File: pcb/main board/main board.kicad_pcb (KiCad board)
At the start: 2 copper layers, 110 x 155 mm, 71 parts, among them J1 Motor 0 Conn, J10 12V Battery, J11 BAU, J12 Servo 4 Conn, J13 Servo 1 Conn, J14 Servo 2 Conn, J15 Servo 3 Conn, J16 Servo 5 Conn, J17 Servo 6 Conn, J18 Servo 7 Conn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

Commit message: Finished PCB !
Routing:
- net +5VP: track 151.5 -> 353.7 mm, vias 2 -> 12
- net +12V: track 302.5 -> 356.2 mm, vias 10 -> 11
- net I2C 0 SDA: track 74.0 -> 96.9 mm, vias 2 -> 4
- net I2C 0 SCL: track 86.2 -> 108.0 mm, vias 4 -> 5
- net +5VL: track 325.6 -> 324.0 mm

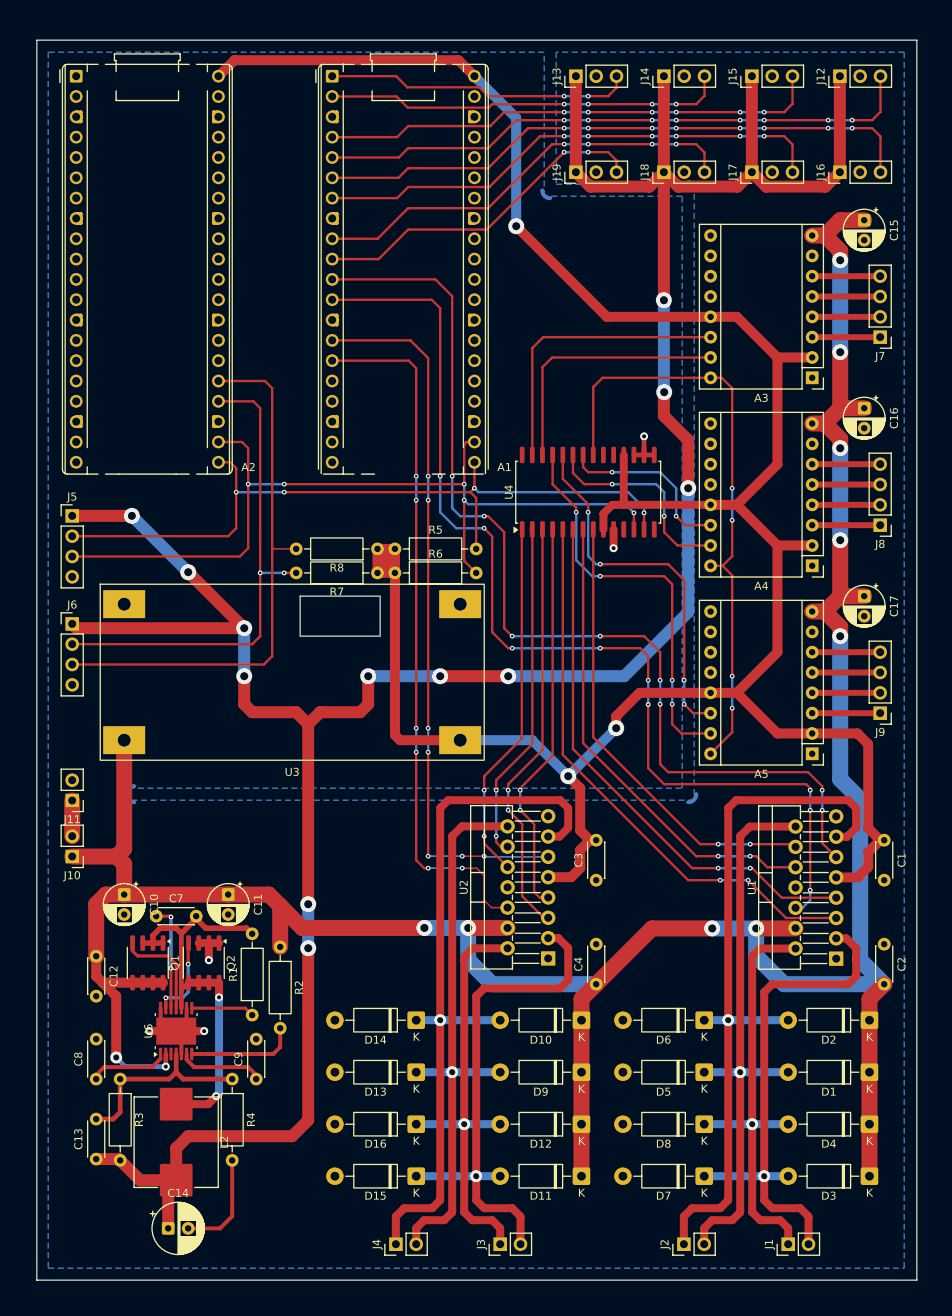
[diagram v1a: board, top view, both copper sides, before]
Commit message: Added Aisler DRC and corrected errors.
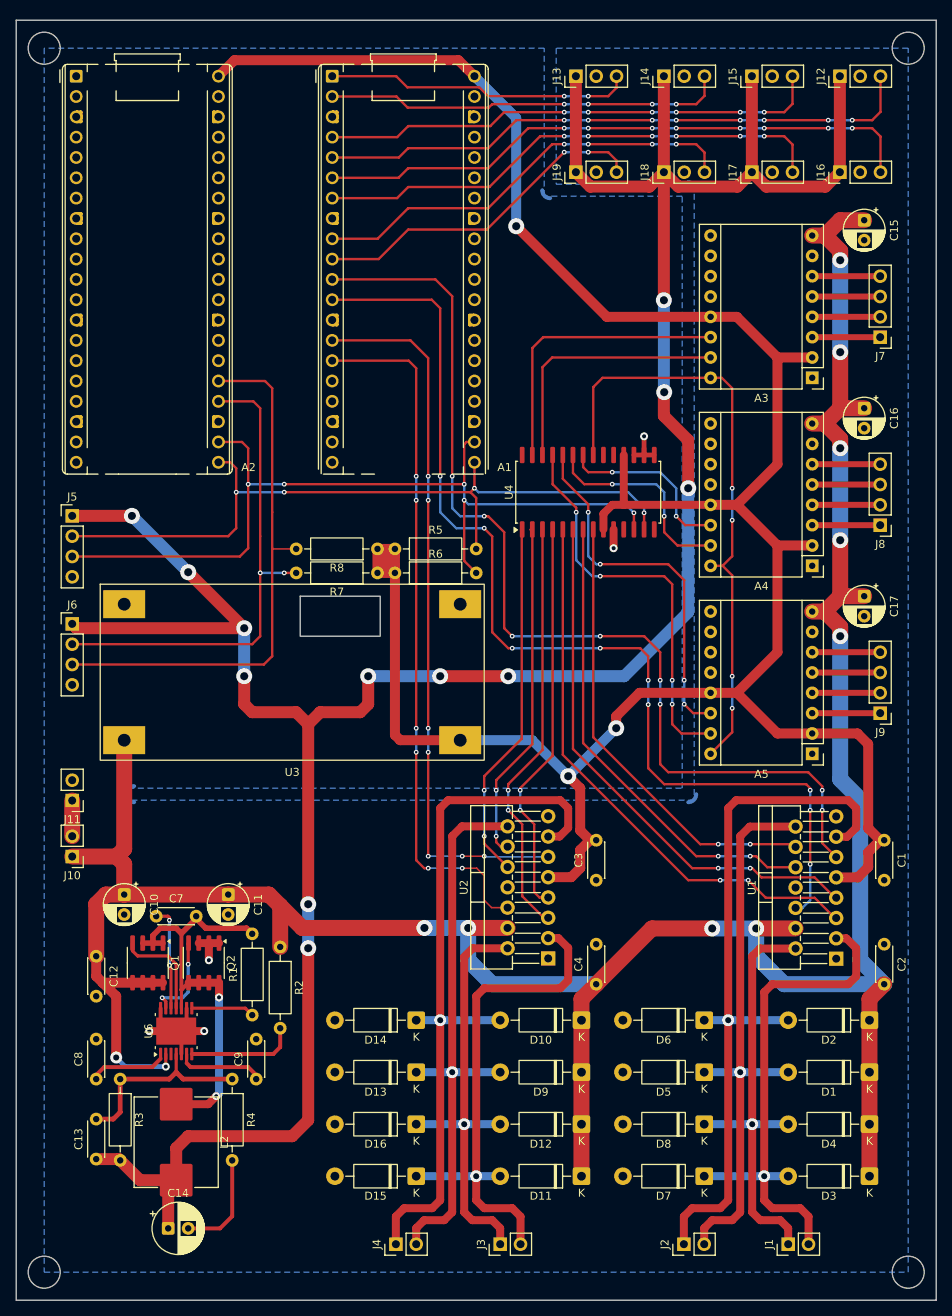
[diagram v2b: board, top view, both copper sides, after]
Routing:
- net Net-(Q2-G): track 10.5 -> 11.2 mm
- net Servo 4 PWM: track 75.9 -> 75.4 mm
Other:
- board size 110 x 155 mm -> 115 x 160 mm

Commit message: Added motors encoders connectors
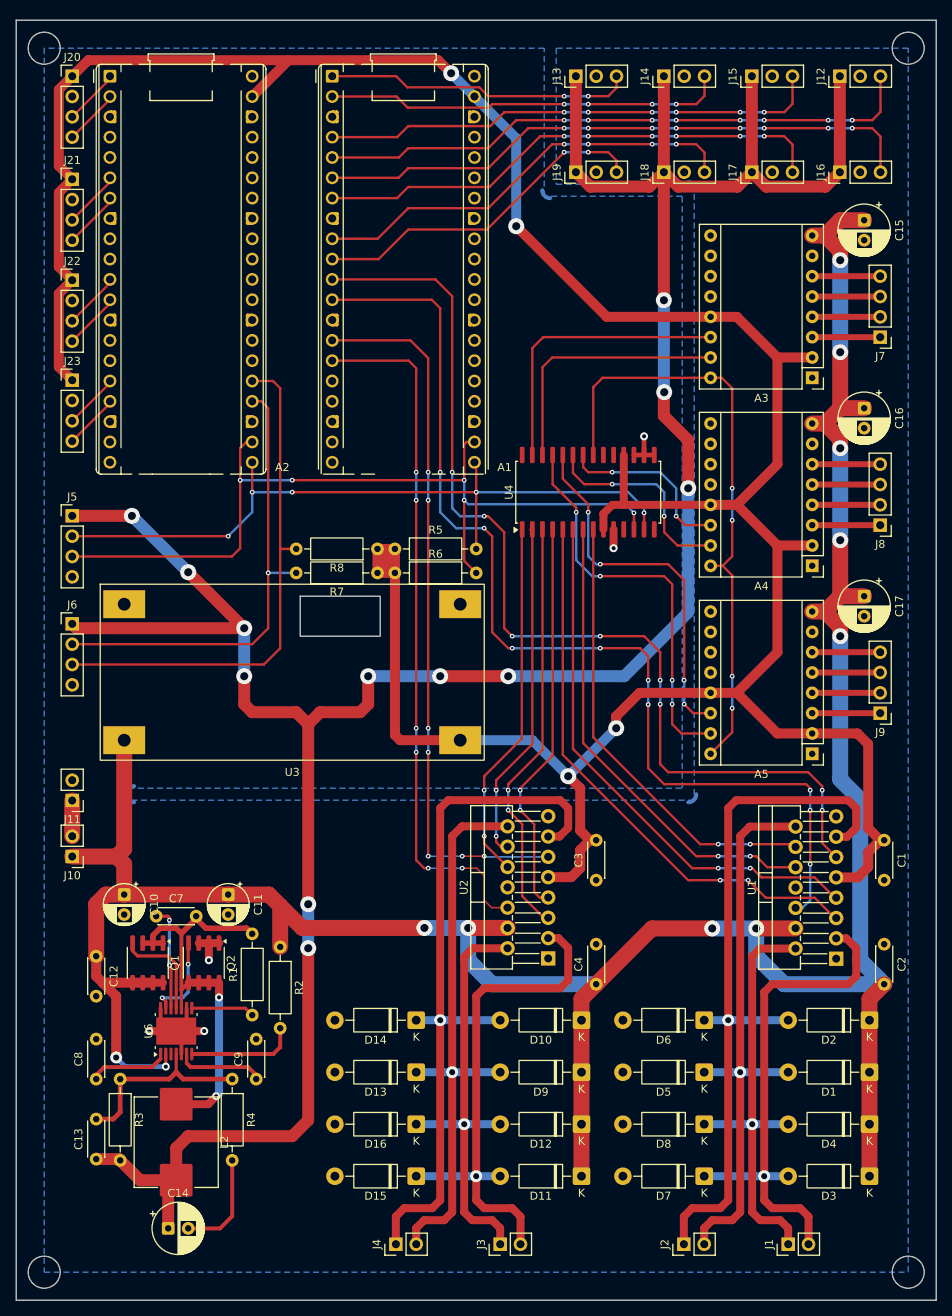
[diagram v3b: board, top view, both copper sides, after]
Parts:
- added J20: Motor 1 Encoder, Connector_PinHeader_2.54mm:PinHeader_1x04_P2.54mm_Vertical, F.Cu at (182.0, 72.0)
- added J21: Motor 2 Encoder, Connector_PinHeader_2.54mm:PinHeader_1x04_P2.54mm_Vertical, F.Cu at (182.0, 84.9)
- added J22: Motor 3 Encoder, Connector_PinHeader_2.54mm:PinHeader_1x04_P2.54mm_Vertical, F.Cu at (182.0, 97.5)
- added J23: Motor 4 Encoder, Connector_PinHeader_2.54mm:PinHeader_1x04_P2.54mm_Vertical, F.Cu at (182.0, 110.0)
- C15, C16, C17: footprint Capacitor_THT:CP_Radial_D5.0mm_P2.50mm -> Capacitor_THT:CP_Radial_D6.3mm_P2.50mm
- moved A2 4.22 mm to (186.7, 72.0)
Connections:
- A1 pad 33: unconnected-(A1-AGND-Pad33) -> GNDPWR
- A1 pad 39: unconnected-(A1-VSYS-Pad39) -> +5VL
- A1 pad 40: +5VL -> unconnected-(A1-VBUS-Pad40)
- A2 pad 1: unconnected-(A2-GPIO0-Pad1) -> Codeur 1 Pin 1
- A2 pad 11: unconnected-(A2-GPIO8-Pad11) -> Codeur 3 Pin 1
- A2 pad 12: unconnected-(A2-GPIO9-Pad12) -> Codeur 3 Pin 2
- A2 pad 16: unconnected-(A2-GPIO12-Pad16) -> Codeur 4 Pin 1
- A2 pad 17: unconnected-(A2-GPIO13-Pad17) -> Codeur 4 Pin 2
- A2 pad 2: unconnected-(A2-GPIO1-Pad2) -> Codeur 1 Pin 2
- A2 pad 39: unconnected-(A2-VSYS-Pad39) -> +5VL
- A2 pad 40: +5VL -> unconnected-(A2-VBUS-Pad40)
- A2 pad 6: unconnected-(A2-GPIO4-Pad6) -> Codeur 2 Pin 1
- A2 pad 7: unconnected-(A2-GPIO5-Pad7) -> Codeur 2 Pin 2
- A3 pad 11: unconnected-(A3-MS2-Pad11) -> GNDPWR
- A3 pad 12: unconnected-(A3-MS3-Pad12) -> GNDPWR
- A4 pad 11: unconnected-(A4-MS2-Pad11) -> GNDPWR
- A4 pad 12: unconnected-(A4-MS3-Pad12) -> GNDPWR
- A5 pad 11: unconnected-(A5-MS2-Pad11) -> GNDPWR
- A5 pad 12: unconnected-(A5-MS3-Pad12) -> GNDPWR
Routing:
- net +5VL: track 324.0 -> 389.4 mm, vias 3 -> 4
- net Codeur 2 Pin 2: track 0.00 -> 7.22 mm
- net Codeur 2 Pin 1: track 0.00 -> 7.22 mm
- net Codeur 3 Pin 2: track 0.00 -> 7.14 mm
- net Codeur 3 Pin 1: track 0.00 -> 7.14 mm
- net Codeur 1 Pin 2: track 0.00 -> 7.04 mm
- net Codeur 1 Pin 1: track 0.00 -> 7.04 mm
- net Codeur 4 Pin 2: track 0.00 -> 6.94 mm
- net Codeur 4 Pin 1: track 0.00 -> 6.94 mm
- net I2C 1 SCL: track 69.1 -> 65.2 mm
- net I2C 1 SDA: track 62.5 -> 58.7 mm, vias 2 -> 1
- net I2C 0 SDA: track 96.9 -> 93.4 mm, vias 4 -> 5
- net I2C 0 SCL: track 108.0 -> 105.8 mm

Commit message: Changed empreinte and rewired them to match commanded ones
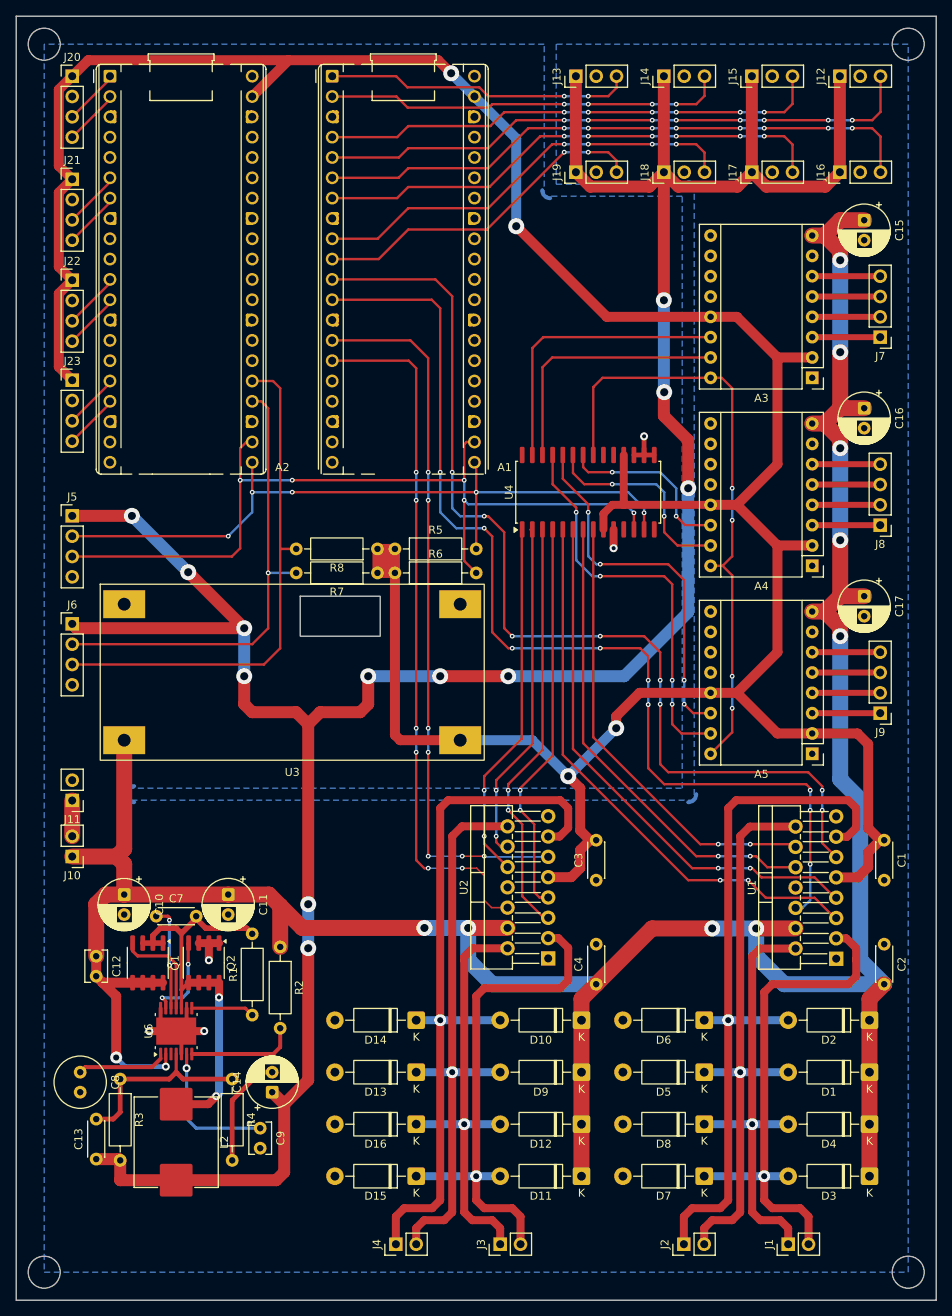
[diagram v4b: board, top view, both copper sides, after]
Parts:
- C10, C11: footprint Capacitor_THT:CP_Radial_D5.0mm_P2.50mm -> Capacitor_THT:CP_Radial_D6.3mm_P2.50mm
- C12, C9: footprint Capacitor_THT:C_Disc_D4.3mm_W1.9mm_P5.00mm -> Capacitor_THT:C_Disc_D3.8mm_W2.6mm_P2.50mm
- C8: footprint Capacitor_THT:C_Disc_D4.3mm_W1.9mm_P5.00mm -> Capacitor_THT:C_Radial_D6.3mm_H5.0mm_P2.50mm
- moved C14 21.4 mm to (207.0, 199.0), turned to 90 degrees
- moved C9 6.16 mm to (205.5, 203.5), turned to -90 degrees
- moved C8 2.18 mm to (183.0, 196.5), turned to -90 degrees
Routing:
- net Net-(U6-SS): track 11.0 -> 17.8 mm, vias 0 -> 1
- net +5VP: track 353.7 -> 350.6 mm
- net Net-(U6-VCC): track 9.99 -> 11.3 mm
- net Net-(C14-Pad2): track 13.1 -> 14.0 mm
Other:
- board size 115 x 160 mm -> 115 x 160.5 mm
